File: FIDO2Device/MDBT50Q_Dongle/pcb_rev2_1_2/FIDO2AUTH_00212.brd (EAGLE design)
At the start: 19.1 x 34.3 mm, 39 parts, among them CN1 TE-1734028, CN2 IF_4PIN, CN5 IF_2PIN_SOL, SW1 SKRPACE010, SW2 SKTADAE010, U1 MDBT50Q-P1M, U2 XC6206P332MR-G, U3 ATECC608A-MAHDA-S, X1 NX3215SA-32.768K

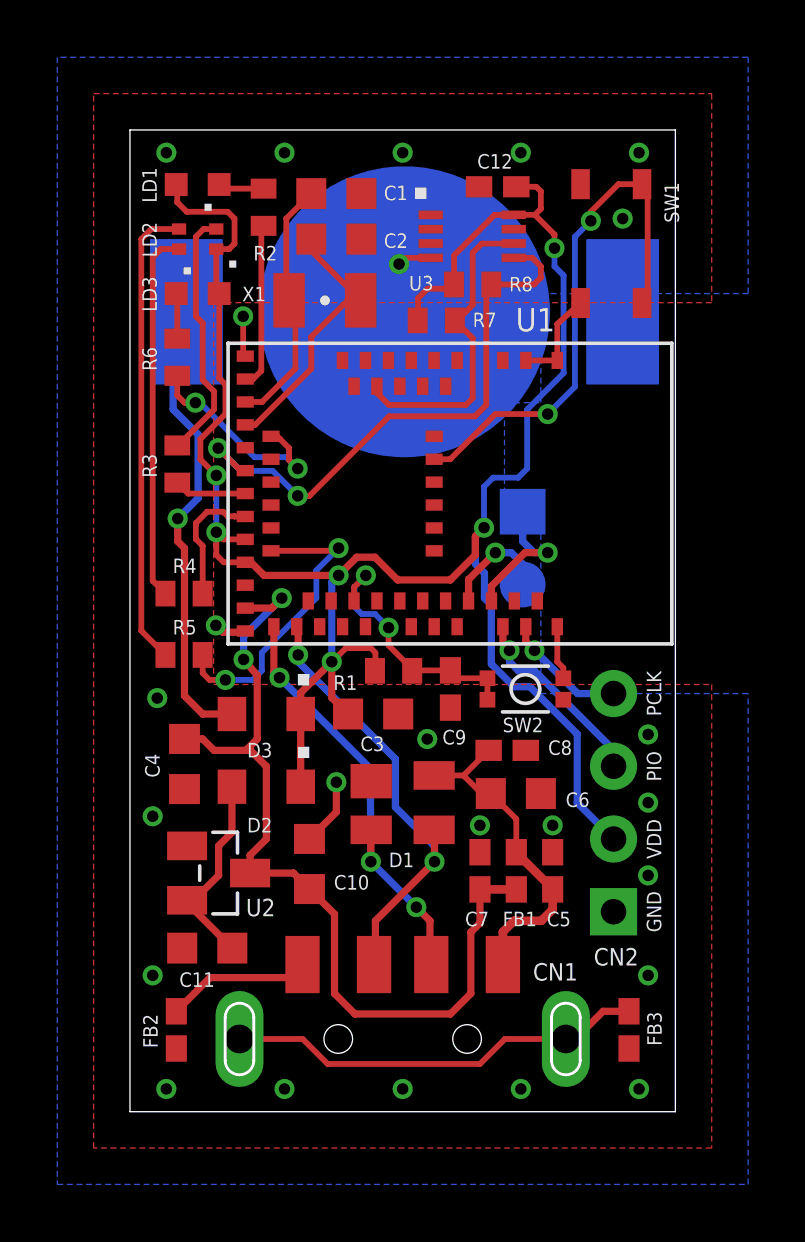
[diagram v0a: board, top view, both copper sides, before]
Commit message: 回路図・レイアウトを修正
・３色LEDを単色LEDに分割
・LEDの部品番号を修正
・旧・LED1（赤色LED）は廃止
・配線／ビア位置を若干見直し
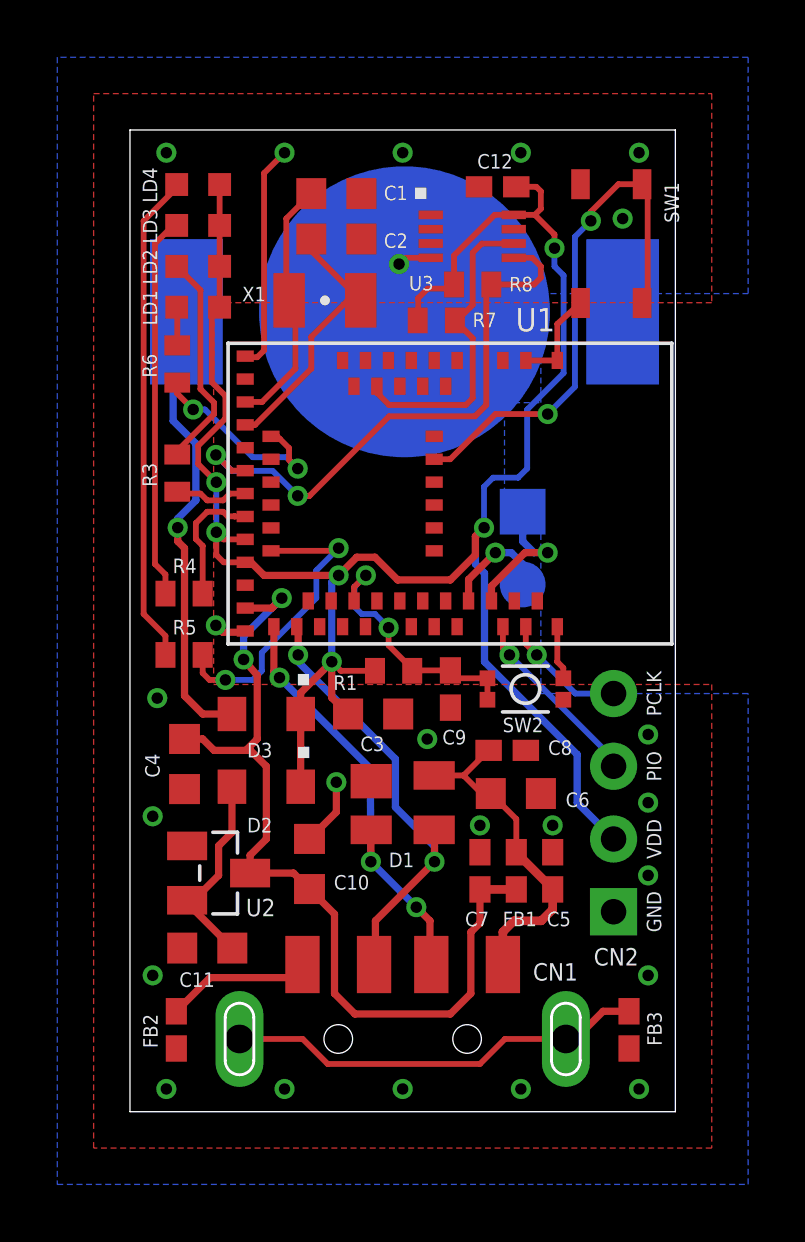
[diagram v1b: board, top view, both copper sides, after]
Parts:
- removed R2: 1.5k, Parts:R0402
- added LD4: APHD1608LQBC/D, Parts:CHIPLED_0603
- LD1: value APHD1608LSURCK -> APTD1608LSYCK
- LD2: value APHF1608LSEEQBDZGKC -> APHD1608LSURCK; device Parts:APHF1608LSEEQBDZGKC -> Parts:CHIPLED_0603
- LD3: value APTD1608LSYCK -> APTD1608LCGCK
- moved LD1 4.29 mm to (2.38, 28.1), turned to 180 degrees
- moved LD3 2.38 mm to (2.38, 31.0)
- moved LD2 0.95 mm to (2.38, 29.5)
- moved R3 0.32 mm to (1.65, 22.3)
- moved R6 0.24 mm to (1.65, 26.1)
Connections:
- net LED2_B renamed LED4
- net LED2_R renamed LED2
- removed net LED2_G: R4.1, U1.26
- removed net N$11: LD1.C, R2.2
- net LED1: now also R6.1, U1.19; no longer R2.1, U1.16
- net LED3: now also R4.1, U1.26; no longer R6.1, U1.19
- net N$1: now also LD4.C, R5.2; no longer LD2.2, R3.2
- net N$6: now also LD3.C; no longer LD2.4
- net N$7: now also LD2.C, R3.2; no longer LD2.3, R5.2
- net N$8: now also LD1.C; no longer LD3.C
- net VDD_NRF: now also LD2.A, LD4.A; no longer LD2.1
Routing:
- net N$7: track 16.3 -> 7.65 mm
- net N$1: track 8.93 -> 17.2 mm
- net 0V: track 11.5 -> 18.1 mm, vias 25 -> 24
- net LED2_G: track 4.52 -> 0.00 mm
- net LED3: track 8.11 -> 4.52 mm, vias 2 -> 0
- net VDD_NRF: track 75.8 -> 73.1 mm
- net LED1: track 5.78 -> 7.67 mm, vias 0 -> 2
- net N$11: track 1.61 -> 0.00 mm

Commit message: 回路図・レイアウトを修正
・LED品番を、入手性の良い物に変更
・LED関連のレイアウトを修正（パターンを修正）
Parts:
- LD1: value APTD1608LSYCK -> APTD1608LSECK/J4-PF; device Parts:CHIPLED_0603 -> Parts:APTD1608
- LD2: device Parts:CHIPLED_0603 -> Parts:APTD1608
- LD3: value APTD1608LCGCK -> APTD1608LZGCK; device Parts:CHIPLED_0603 -> Parts:APTD1608
- LD4: value APHD1608LQBC/D -> APTD1608LVBC/D; device Parts:CHIPLED_0603 -> Parts:APTD1608
- moved LD1 0.16 mm to (2.54, 28.1)
- moved LD2 0.16 mm to (2.54, 29.5)
- moved LD3 0.16 mm to (2.54, 31.0)
- moved LD4 0.16 mm to (2.54, 32.4)
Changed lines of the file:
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@@
 <layer number="42" name="bRestrict" color="1" fill="10" visible="no" active="yes"/>
 <layer number="43" name="vRestrict" color="2" fill="10" visible="no" active="yes"/>
-<layer number="44" name="Drills" color="7" fill="1" visible="yes" active="yes"/>
+<layer number="44" name="Drills" color="7" fill="1" visible="no" active="yes"/>
 <layer number="45" name="Holes" color="7" fill="1" visible="yes" active="yes"/>
 <layer number="46" name="Milling" color="3" fill="1" visible="yes" active="yes"/>
@@
 </element>
 <element name="X1" library="Parts" package="NX3215" value="NX3215SA-32.768K" x="6.810375" y="28.336875" smashed="yes">
-<attribute name="NAME" x="4.746625" y="28.813125" size="0.508" layer="25" rot="R180"/>
+<attribute name="NAME" x="4.587875" y="29.606875" size="0.508" layer="25"/>
 <attribute name="VALUE" x="4.985375" y="26.286875" size="0.8128" layer="27"/>
 </element>
@@
 </element>
 <element name="BAT1" library="Connectors" package="BAT-HLD-012-SMT" value="BAT-HLD-012-SMT" x="9.5885" y="27.94" rot="MR180"/>
-<element name="LD1" library="Parts" package="CHIPLED_0603" value="APTD1608LSYCK" x="2.38125" y="28.09875" smashed="yes" rot="R180">
+<element name="LD1" library="Parts" package="APTD1608" value="APTD1608LSECK/J4-PF" x="2.54" y="28.09875" smashed="yes" rot="R180">
 <attribute name="NAME" x="0.9525" y="27.46375" size="0.508" layer="25" rot="R90"/>
-<attribute name="VALUE" x="3.175" y="30.00375" size="0.7112" layer="27" rot="R180"/>
+<attribute name="VALUE" x="3.33375" y="30.00375" size="0.7112" layer="27" rot="R180"/>
 </element>
 <element name="R6" library="Parts" package="R0402" value="1.5k" x="1.651" y="26.114375" smashed="yes" rot="R90">
@@
 <attribute name="VALUE" x="12.525375" y="30.32125" size="0.7112" layer="27" rot="R180"/>
 </element>
-<element name="LD3" library="Parts" package="CHIPLED_0603" value="APTD1608LCGCK" x="2.38125" y="30.95625" smashed="yes" rot="R180">
+<element name="LD3" library="Parts" package="APTD1608" value="APTD1608LZGCK" x="2.54" y="30.95625" smashed="yes" rot="R180">
 <attribute name="NAME" x="0.9525" y="30.32125" size="0.508" layer="25" rot="R90"/>
-<attribute name="VALUE" x="3.175" y="32.96125" size="0.7112" layer="27" rot="R180"/>
-</element>
-<element name="LD2" library="Parts" package="CHIPLED_0603" value="APHD1608LSURCK" x="2.38125" y="29.5275" smashed="yes" rot="R180">
+<attribute name="VALUE" x="3.33375" y="32.96125" size="0.7112" layer="27" rot="R180"/>
+</element>
+<element name="LD2" library="Parts" package="APTD1608" value="APHD1608LSURCK" x="2.54" y="29.5275" smashed="yes" rot="R180">
 <attribute name="NAME" x="0.9525" y="28.8925" size="0.508" layer="25" rot="R90"/>
-<attribute name="VALUE" x="3.175" y="31.5325" size="0.7112" layer="27" rot="R180"/>
-</element>
-<element name="LD4" library="Parts" package="CHIPLED_0603" value="APHD1608LQBC/D" x="2.38125" y="32.385" smashed="yes" rot="R180">
+<attribute name="VALUE" x="3.33375" y="31.5325" size="0.7112" layer="27" rot="R180"/>
+</element>
+<element name="LD4" library="Parts" package="APTD1608" value="APTD1608LVBC/D" x="2.54" y="32.385" smashed="yes" rot="R180">
 <attribute name="NAME" x="0.9525" y="31.75" size="0.508" layer="25" rot="R90"/>
-<attribute name="VALUE" x="3.175" y="34.39" size="0.7112" layer="27" rot="R180"/>
+<attribute name="VALUE" x="3.33375" y="34.39" size="0.7112" layer="27" rot="R180"/>
 </element>
 </elements>
@@
 <contactref element="LD2" pad="A"/>
 <contactref element="LD4" pad="A"/>
-<wire x1="3.33375" y1="27.89625" x2="3.13125" y2="28.09875" width="0.2032" layer="1"/>
+<wire x1="3.33375" y1="27.89625" x2="3.34" y2="28.09875" width="0.2032" layer="1"/>
 <wire x1="3.01625" y1="21.986875" x2="2.38125" y2="22.621875" width="0.2032" layer="1"/>
 <wire x1="2.38125" y1="22.621875" x2="2.38125" y2="23.256875" width="0.2032" layer="1"/>
 <wire x1="3.33375" y1="24.209375" x2="2.38125" y2="23.256875" width="0.2032" layer="1"/>
-<wire x1="3.13125" y1="28.09875" x2="3.13125" y2="29.5275" width="0.2032" layer="1"/>
-<wire x1="3.13125" y1="29.5275" x2="3.13125" y2="30.95625" width="0.2032" layer="1"/>
-<wire x1="3.13125" y1="30.95625" x2="3.13125" y2="32.385" width="0.2032" layer="1"/>
+<wire x1="3.34" y1="29.5275" x2="3.34" y2="30.95625" width="0.2032" layer="1"/>
+<wire x1="3.34" y1="30.95625" x2="3.34" y2="32.385" width="0.2032" layer="1"/>
 <wire x1="3.33375" y1="24.209375" x2="3.33375" y2="25.003125" width="0.2032" layer="1"/>
 <wire x1="3.33375" y1="25.003125" x2="2.8575" y2="25.479375" width="0.2032" layer="1"/>
-<wire x1="2.8575" y1="25.479375" x2="2.8575" y2="27.825" width="0.2032" layer="1"/>
-<wire x1="2.8575" y1="27.825" x2="3.13125" y2="28.09875" width="0.2032" layer="1"/>
 <wire x1="8.5575" y1="15.39875" x2="7.366" y2="15.39875" width="0.2032" layer="1"/>
 <wire x1="7.366" y1="15.39875" x2="7.0485" y2="15.71625" width="0.2032" layer="1"/>
@@
 <wire x1="15.621" y1="12.47775" x2="12.3825" y2="15.71625" width="0.254" layer="16"/>
 <wire x1="12.3825" y1="18.811875" x2="12.3825" y2="15.71625" width="0.254" layer="16"/>
+<wire x1="2.8575" y1="25.479375" x2="2.8575" y2="27.61625" width="0.2032" layer="1"/>
+<wire x1="2.8575" y1="27.61625" x2="3.34" y2="28.09875" width="0.2032" layer="1"/>
+<wire x1="3.34" y1="29.5275" x2="3.34" y2="28.09875" width="0.2032" layer="1"/>
 </signal>
 <signal name="VBUS">
@@
 <contactref element="LD1" pad="C"/>
 <contactref element="R6" pad="2"/>
-<wire x1="1.651" y1="26.764375" x2="1.651" y2="28.079" width="0.2032" layer="1"/>
-<wire x1="1.651" y1="28.079" x2="1.63125" y2="28.09875" width="0.2032" layer="1"/>
+<wire x1="1.651" y1="26.764375" x2="1.651" y2="28.00975" width="0.2032" layer="1"/>
+<wire x1="1.651" y1="28.00975" x2="1.74" y2="28.09875" width="0.2032" layer="1"/>
 </signal>
 <signal name="TWI_SDA">
@@
 <wire x1="1.239125" y1="16.62025" x2="0.47625" y2="17.383125" width="0.2032" layer="1"/>
 <wire x1="0.47625" y1="17.383125" x2="0.47625" y2="31.115" width="0.2032" layer="1"/>
-<wire x1="1.63125" y1="32.385" x2="1.63125" y2="32.27" width="0.2032" layer="1"/>
+<wire x1="1.74" y1="32.385" x2="1.63125" y2="32.27" width="0.2032" layer="1"/>
 <wire x1="1.63125" y1="32.27" x2="0.47625" y2="31.115" width="0.2032" layer="1"/>
 </signal>
@@
 <contactref element="LD3" pad="C"/>
 <wire x1="0.873125" y1="19.129375" x2="0.873125" y2="30.32125" width="0.2032" layer="1"/>
-<wire x1="1.63125" y1="30.95625" x2="1.508125" y2="30.95625" width="0.2032" layer="1"/>
+<wire x1="1.74" y1="30.95625" x2="1.508125" y2="30.95625" width="0.2032" layer="1"/>
 <wire x1="1.508125" y1="30.95625" x2="0.873125" y2="30.32125" width="0.2032" layer="1"/>
 <wire x1="1.239125" y1="18.0975" x2="1.239125" y2="18.763375" width="0.2032" layer="1"/>
@@
 <wire x1="2.936875" y1="24.368125" x2="2.936875" y2="24.765" width="0.2032" layer="1"/>
 <wire x1="2.936875" y1="24.765" x2="2.460625" y2="25.24125" width="0.2032" layer="1"/>
-<wire x1="2.460625" y1="25.24125" x2="2.460625" y2="28.698125" width="0.2032" layer="1"/>
-<wire x1="2.460625" y1="28.698125" x2="1.63125" y2="29.5275" width="0.2032" layer="1"/>
+<wire x1="2.460625" y1="25.24125" x2="2.460625" y2="29.289375" width="0.2032" layer="1"/>
+<wire x1="1.74" y1="29.5275" x2="2.2225" y2="29.5275" width="0.2032" layer="1"/>
+<wire x1="2.2225" y1="29.5275" x2="2.460625" y2="29.289375" width="0.2032" layer="1"/>
 </signal>
 </signals>

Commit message: 回路図を修正
・LED用抵抗器の定数を修正
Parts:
- R4: value 2.2k -> 390
- R6: value 1.5k -> 1.2k
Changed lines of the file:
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@@
 <attribute name="VALUE" x="3.2385" y="21.669375" size="0.7112" layer="27" rot="R90"/>
 </element>
-<element name="R4" library="Parts" package="R0402" value="2.2k" x="1.889125" y="18.0975" smashed="yes" rot="R180">
+<element name="R4" library="Parts" package="R0402" value="390" x="1.889125" y="18.0975" smashed="yes" rot="R180">
 <attribute name="NAME" x="1.49225" y="18.811875" size="0.508" layer="25"/>
 <attribute name="VALUE" x="2.524125" y="19.685" size="0.7112" layer="27" rot="R180"/>
@@
 <attribute name="VALUE" x="3.33375" y="30.00375" size="0.7112" layer="27" rot="R180"/>
 </element>
-<element name="R6" library="Parts" package="R0402" value="1.5k" x="1.651" y="26.114375" smashed="yes" rot="R90">
+<element name="R6" library="Parts" package="R0402" value="1.2k" x="1.651" y="26.114375" smashed="yes" rot="R90">
 <attribute name="NAME" x="0.936625" y="25.638125" size="0.508" layer="25" rot="R90"/>
 <attribute name="VALUE" x="3.2385" y="25.479375" size="0.7112" layer="27" rot="R90"/>
